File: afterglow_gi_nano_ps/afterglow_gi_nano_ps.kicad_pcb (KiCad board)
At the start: 2 copper layers, 84 x 134.5 mm, 69 parts, among them J1 Conn_02x17_Odd_Even, J2 POWER_CONN, J3 GI_WPC_J120, J4 GI_WPC_J121, J5 GI_CONN_J119, J6 Conn_01x12_Male, Q1 FQP30N06L, Q2 FQP30N06L, Q3 FQP30N06L, Q4 FQP30N06L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

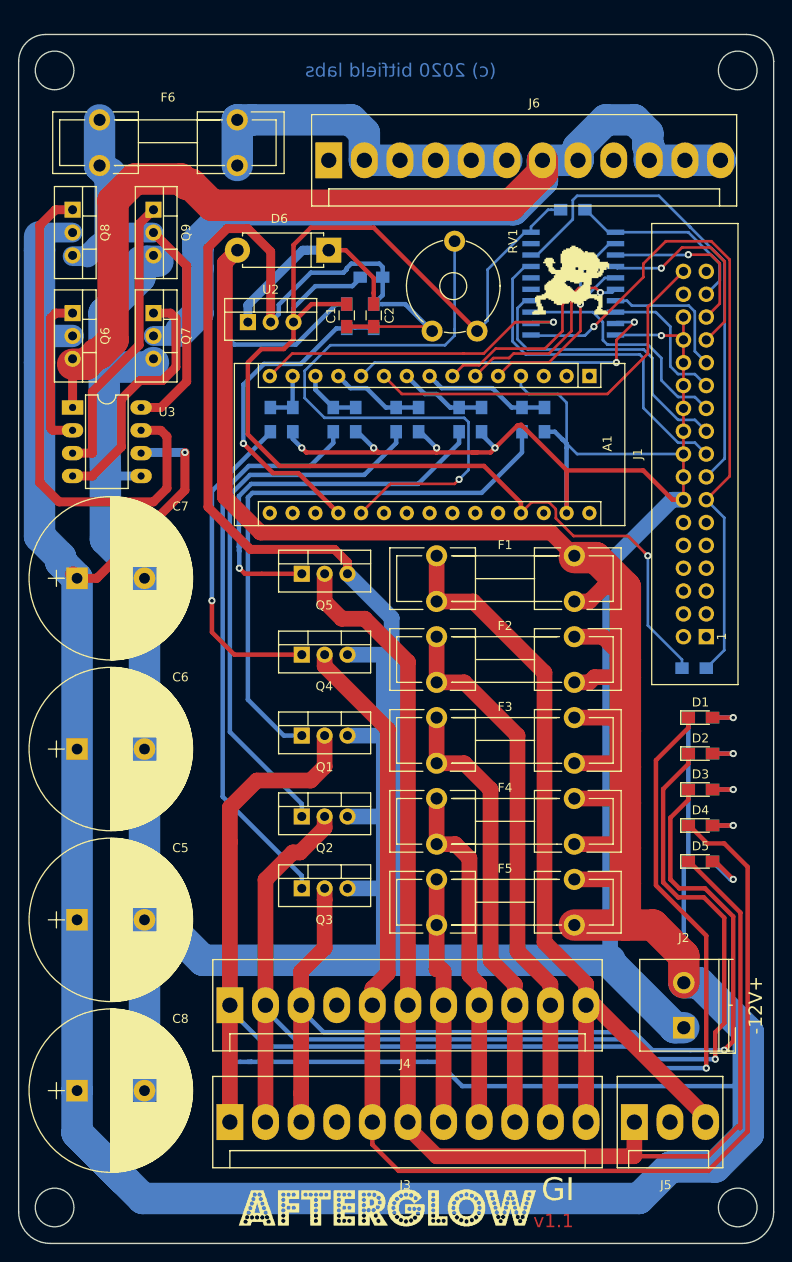
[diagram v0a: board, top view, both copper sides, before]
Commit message: New power supply
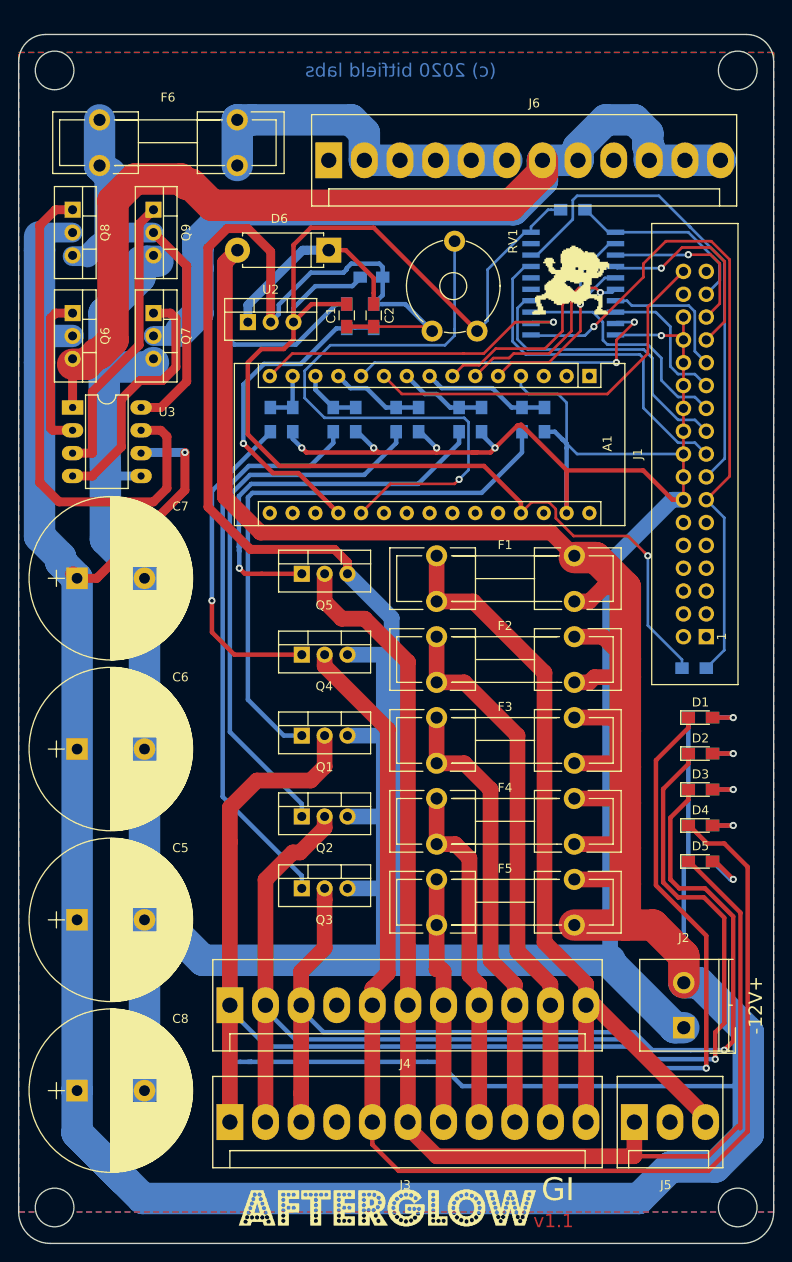
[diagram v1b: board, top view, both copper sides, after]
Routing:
- added copper zone on B.Cu, net GND
- added copper zone on F.Cu, net GND
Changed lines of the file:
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@@
   (segment (start 48.899999 32.100001) (end 50.5 30.5) (width 1) (layer F.Cu) (net 90))
   (segment (start 43.7 57.58) (end 43.7 50.764836) (width 1) (layer F.Cu) (net 90))
+  (zone (net 1) (net_name GND) (layer B.Cu) (hatch edge 0.508)
+    (connect_pads (clearance 0.508))
+    (min_thickness 0.254)
+    (fill yes (arc_segments 32) (thermal_gap 0.508) (thermal_bridge_width 0.508))
+    (polygon
+      (pts
+        (xy 119.5 142) (xy 35.5 142) (xy 35.5 13) (xy 119.5 13)
+      )
+    )
+  )
+  (zone (net 1) (net_name GND) (layer F.Cu) (hatch edge 0.508)
+    (connect_pads (clearance 0.508))
+    (min_thickness 0.254)
+    (fill yes (arc_segments 32) (thermal_gap 0.508) (thermal_bridge_width 0.508))
+    (polygon
+      (pts
+        (xy 119.5 142) (xy 35.5 142) (xy 35.5 13) (xy 119.5 13)
+      )
+    )
+  )
 )

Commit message: PCB cosmetix
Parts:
- F6 - 10A: renamed from F6
- J115 IN: renamed from J6
- J119 OUT: renamed from J5
- J120 OUT: renamed from J3
- J121 OUT: renamed from J4
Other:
- board text added: "2A"
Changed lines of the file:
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@@
   (general
     (thickness 1.6)
-    (drawings 16)
+    (drawings 21)
     (tracks 711)
     (zones 0)
@@
   )
   (setup
-    (last_trace_width 1)
+    (last_trace_width 0.5)
     (user_trace_width 1)
     (user_trace_width 1.75)
@@
     (pcbplotparams
       (layerselection 0x010fc_ffffffff)
-      (usegerberextensions false)
+      (usegerberextensions true)
       (usegerberattributes false)
       (usegerberadvancedattributes false)
@@
     (descr "Connector Headers with Friction Lock, 26-60-4020, http://www.molex.com/pdm_docs/sd/026604020_sd.pdf")
     (tags "connector molex kk_41791 26-60-4020")
-    (fp_text reference J6 (at 22.86 -6.35) (layer F.SilkS)
+    (fp_text reference "J115 IN" (at 22.5 -7) (layer F.SilkS)
       (effects (font (size 1 1) (thickness 0.15)))
     )
@@
     (descr "Fuseholder, 5x20, open, horizontal, Type-II, lateral,")
     (tags "Fuseholder 5x20 open horizontal Type-II lateral Sicherungshalter offen ")
-    (fp_text reference F6 (at 7.61 -2.5) (layer F.SilkS)
+    (fp_text reference "F6 - 10A" (at 7.61 -3) (layer F.SilkS)
       (effects (font (size 1 1) (thickness 0.15)))
     )
@@
     (descr "Connector Headers with Friction Lock, 26-60-4020, http://www.molex.com/pdm_docs/sd/026604020_sd.pdf")
     (tags "connector molex kk_41791 26-60-4020")
-    (fp_text reference J3 (at 19.5 7) (layer F.SilkS)
+    (fp_text reference "J120 OUT" (at 19.5 6.5) (layer F.SilkS)
       (effects (font (size 1 1) (thickness 0.15)))
     )
@@
     (descr "Connector Headers with Friction Lock, 26-60-4020, http://www.molex.com/pdm_docs/sd/026604020_sd.pdf")
     (tags "connector molex kk_41791 26-60-4020")
-    (fp_text reference J4 (at 19.5 6.5) (layer F.SilkS)
+    (fp_text reference "J121 OUT" (at 19.5 6.5) (layer F.SilkS)
       (effects (font (size 1 1) (thickness 0.15)))
     )
@@
     (descr "Connector Headers with Friction Lock, 26-60-4020, http://www.molex.com/pdm_docs/sd/026604020_sd.pdf")
     (tags "connector molex kk_41791 26-60-4020")
-    (fp_text reference J5 (at 3.5 7) (layer F.SilkS)
+    (fp_text reference "J119 OUT" (at 3.5 6.5) (layer F.SilkS)
       (effects (font (size 1 1) (thickness 0.15)))
     )
@@
       (xy 18.3 0)) (layer F.SilkS) (width 0.01))
   )
+  (gr_text 2A (at 89.5 106.5) (layer F.SilkS)
+    (effects (font (size 1 1) (thickness 0.15)))
+  )
+  (gr_text 2A (at 89.5 97.5) (layer F.SilkS)
+    (effects (font (size 1 1) (thickness 0.15)))
+  )
+  (gr_text 2A (at 89.5 88.5) (layer F.SilkS)
+    (effects (font (size 1 1) (thickness 0.15)))
+  )
+  (gr_text 2A (at 89.5 79.5) (layer F.SilkS)
+    (effects (font (size 1 1) (thickness 0.15)))
+  )
+  (gr_text 2A (at 89.5 70.5) (layer F.SilkS)
+    (effects (font (size 1 1) (thickness 0.15)))
+  )
   (dimension 84.001488 (width 0.3) (layer F.SilkS)

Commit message: Added missing C4 footprint, grounding pads
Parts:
- removed the ? at (39.5, 141.5)
- removed the ? at (115.5, 15.0)
- added C4: C, Capacitors_THT:C_Rect_L7.0mm_W3.5mm_P5.00mm, F.Cu at (60.0, 89.0)
- added REF**: MountingHole_4.3mm_M4_Pad, Mounting_Holes:MountingHole_4.3mm_M4_Pad, F.Cu at (115.0, 15.5)
- added REF**: MountingHole_4.3mm_M4_Pad, Mounting_Holes:MountingHole_4.3mm_M4_Pad, F.Cu at (40.0, 141.0)
- F6: renamed from F6 - 10A
- J3: renamed from J120 OUT
- J4: renamed from J121 OUT
- J5: renamed from J119 OUT
- J6: renamed from J115 IN
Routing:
- net +12V: track 551.1 -> 574.0 mm
- net GND: track 526.3 -> 539.5 mm
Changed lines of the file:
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@@
     (thickness 1.6)
     (drawings 21)
-    (tracks 711)
+    (tracks 718)
     (zones 0)
-    (modules 69)
+    (modules 70)
     (nets 91)
   )
@@
   )
   (setup
-    (last_trace_width 0.5)
+    (last_trace_width 1.75)
     (user_trace_width 1)
     (user_trace_width 1.75)
@@
     (add_net "Net-(F5-Pad1)")
   )
+  (module Mounting_Holes:MountingHole_4.3mm_M4_Pad (layer F.Cu)
+    (at 115 15.5)
+    (descr "Mounting Hole 4.3mm, M4")
+    (tags "mounting hole 4.3mm m4")
+    (fp_text reference REF** (at 0 -5.3) (layer F.SilkS)
+      (effects (font (size 1 1) (thickness 0.15)))
+    )
+    (fp_text value MountingHole_4.3mm_M4_Pad (at 0 5.3) (layer F.Fab)
+      (effects (font (size 1 1) (thickness 0.15)))
+    )
+    (fp_circle (center 0 0) (end 4.55 0) (layer F.CrtYd) (width 0.05))
+    (fp_circle (center 0 0) (end 4.3 0) (layer Cmts.User) (width 0.15))
+    (pad 1 thru_hole circle (at 0 0) (size 8.6 8.6) (drill 4.3) (layers *.Cu *.Mask))
+  )
+  (module Mounting_Holes:MountingHole_4.3mm_M4_Pad (layer F.Cu)
+    (at 40 141)
+    (descr "Mounting Hole 4.3mm, M4")
+    (tags "mounting hole 4.3mm m4")
+    (fp_text reference REF** (at 0 -5.3) (layer F.SilkS)
+      (effects (font (size 1 1) (thickness 0.15)))
+    )
+    (fp_text value MountingHole_4.3mm_M4_Pad (at 0 5.3) (layer F.Fab)
+      (effects (font (size 1 1) (thickness 0.15)))
+    )
+    (fp_circle (center 0 0) (end 4.55 0) (layer F.CrtYd) (width 0.05))
+    (fp_circle (center 0 0) (end 4.3 0) (layer Cmts.User) (width 0.15))
+    (pad 1 thru_hole circle (at 0 0) (size 8.6 8.6) (drill 4.3) (layers *.Cu *.Mask))
+  )
+  (module Capacitors_THT:C_Rect_L7.0mm_W3.5mm_P5.00mm (layer F.Cu)
+    (at 60 89 90)
+    (descr "C, Rect series, Radial, pin pitch=5.00mm, , length*width=7*3.5mm^2, Capacitor")
+    (tags "C Rect series Radial pin pitch 5.00mm  length 7mm width 3.5mm Capacitor")
+    (fp_text reference C4 (at 2.5 -3.06 90) (layer F.SilkS)
+      (effects (font (size 1 1) (thickness 0.15)))
+    )
+    (fp_text value C (at 2.5 3.06 90) (layer F.Fab)
+      (effects (font (size 1 1) (thickness 0.15)))
+    )
+    (fp_text user %R (at 2.5 0 90) (layer F.Fab)
+      (effects (font (size 1 1) (thickness 0.15)))
+    )
+    (fp_line (start 6.35 -2.1) (end -1.35 -2.1) (layer F.CrtYd) (width 0.05))
+    (fp_line (start 6.35 2.1) (end 6.35 -2.1) (layer F.CrtYd) (width 0.05))
+    (fp_line (start -1.35 2.1) (end 6.35 2.1) (layer F.CrtYd) (width 0.05))
+    (fp_line (start -1.35 -2.1) (end -1.35 2.1) (layer F.CrtYd) (width 0.05))
+    (fp_line (start 6.06 -1.81) (end 6.06 1.81) (layer F.SilkS) (width 0.12))
+    (fp_line (start -1.06 -1.81) (end -1.06 1.81) (layer F.SilkS) (width 0.12))
+    (fp_line (start -1.06 1.81) (end 6.06 1.81) (layer F.SilkS) (width 0.12))
+    (fp_line (start -1.06 -1.81) (end 6.06 -1.81) (layer F.SilkS) (width 0.12))
+    (fp_line (start 6 -1.75) (end -1 -1.75) (layer F.Fab) (width 0.1))
+    (fp_line (start 6 1.75) (end 6 -1.75) (layer F.Fab) (width 0.1))
+    (fp_line (start -1 1.75) (end 6 1.75) (layer F.Fab) (width 0.1))
+    (fp_line (start -1 -1.75) (end -1 1.75) (layer F.Fab) (width 0.1))
+    (pad 2 thru_hole circle (at 5 0 90) (size 1.6 1.6) (drill 0.8) (layers *.Cu *.Mask)
+      (net 1 GND))
+    (pad 1 thru_hole circle (at 0 0 90) (size 1.6 1.6) (drill 0.8) (layers *.Cu *.Mask)
+      (net 3 +12V))
+    (model ${KISYS3DMOD}/Capacitors_THT.3dshapes/C_Rect_L7.0mm_W3.5mm_P5.00mm.wrl
+      (at (xyz 0 0 0))
+      (scale (xyz 1 1 1))
+      (rotate (xyz 0 0 0))
+    )
+  )
   (module Housings_DIP:DIP-8_W7.62mm_LongPads (layer F.Cu)
     (at 41.5 52.5)
@@
     (descr "Connector Headers with Friction Lock, 26-60-4020, http://www.molex.com/pdm_docs/sd/026604020_sd.pdf")
     (tags "connector molex kk_41791 26-60-4020")
-    (fp_text reference "J115 IN" (at 22.5 -7) (layer F.SilkS)
+    (fp_text reference J6 (at 22.5 -7) (layer F.SilkS)
       (effects (font (size 1 1) (thickness 0.15)))
     )
@@
     (descr "Fuseholder, 5x20, open, horizontal, Type-II, lateral,")
     (tags "Fuseholder 5x20 open horizontal Type-II lateral Sicherungshalter offen ")
-    (fp_text reference "F6 - 10A" (at 7.61 -3) (layer F.SilkS)
+    (fp_text reference F6 (at 7.61 -3) (layer F.SilkS)
       (effects (font (size 1 1) (thickness 0.15)))
     )
@@
   )
   (module Mounting_Holes:MountingHole_4.3mm_M4_DIN965 (layer F.Cu)
-    (at 39.5 141.5)
-    (descr "Mounting Hole 4.3mm, no annular, M4, DIN965")
-    (tags "mounting hole 4.3mm no annular m4 din965")
-    (fp_text reference "" (at 0 -4.75) (layer F.SilkS)
-      (effects (font (size 1 1) (thickness 0.15)))
-    )
-    (fp_text value MountingHole_4.3mm_M4_DIN965 (at 0 4.75) (layer F.Fab)
-      (effects (font (size 1 1) (thickness 0.15)))
-    )
-    (fp_circle (center 0 0) (end 4 0) (layer F.CrtYd) (width 0.05))
-    (fp_circle (center 0 0) (end 3.75 0) (layer Cmts.User) (width 0.15))
-    (pad 1 np_thru_hole circle (at 0 0) (size 4.3 4.3) (drill 4.3) (layers *.Cu *.Mask))
-  )
-  (module Mounting_Holes:MountingHole_4.3mm_M4_DIN965 (layer F.Cu)
     (at 115.5 141.5)
     (descr "Mounting Hole 4.3mm, no annular, M4, DIN965")
@@
     (descr "Connector Headers with Friction Lock, 26-60-4020, http://www.molex.com/pdm_docs/sd/026604020_sd.pdf")
     (tags "connector molex kk_41791 26-60-4020")
-    (fp_text reference "J120 OUT" (at 19.5 6.5) (layer F.SilkS)
+    (fp_text reference J3 (at 19.5 6.5) (layer F.SilkS)
       (effects (font (size 1 1) (thickness 0.15)))
     )
@@
     (descr "Connector Headers with Friction Lock, 26-60-4020, http://www.molex.com/pdm_docs/sd/026604020_sd.pdf")
     (tags "connector molex kk_41791 26-60-4020")
-    (fp_text reference "J121 OUT" (at 19.5 6.5) (layer F.SilkS)
+    (fp_text reference J4 (at 19.5 6.5) (layer F.SilkS)
       (effects (font (size 1 1) (thickness 0.15)))
     )
@@
     (descr "Connector Headers with Friction Lock, 26-60-4020, http://www.molex.com/pdm_docs/sd/026604020_sd.pdf")
     (tags "connector molex kk_41791 26-60-4020")
-    (fp_text reference "J119 OUT" (at 3.5 6.5) (layer F.SilkS)
+    (fp_text reference J5 (at 3.5 6.5) (layer F.SilkS)
       (effects (font (size 1 1) (thickness 0.15)))
     )
@@
     )
   )
-  (module Mounting_Holes:MountingHole_4.3mm_M4_DIN965 (layer F.Cu)
-    (at 115.5 15)
-    (descr "Mounting Hole 4.3mm, no annular, M4, DIN965")
-    (tags "mounting hole 4.3mm no annular m4 din965")
-    (fp_text reference "" (at 0 -4.75) (layer F.SilkS)
-      (effects (font (size 1 1) (thickness 0.15)))
-    )
-    (fp_text value MountingHole_4.3mm_M4_DIN965 (at 0 4.75) (layer F.Fab)
-      (effects (font (size 1 1) (thickness 0.15)))
-    )
-    (fp_circle (center 0 0) (end 4 0) (layer F.CrtYd) (width 0.05))
-    (fp_circle (center 0 0) (end 3.75 0) (layer Cmts.User) (width 0.15))
-    (pad 1 np_thru_hole circle (at 0 0) (size 4.3 4.3) (drill 4.3) (layers *.Cu *.Mask))
-  )
   (module FLAKIE:FLAKIE_inv (layer F.Cu)
     (at 92.5 34.5)
@@
   (segment (start 49.12 60.12) (end 45.294351 60.12) (width 1) (layer B.Cu) (net 1))
   (segment (start 45.152328 59.977977) (end 45 48) (width 3.5) (layer B.Cu) (net 1))
+  (segment (start 56 84) (end 49.5 90.5) (width 1.75) (layer F.Cu) (net 1))
+  (segment (start 60 84) (end 56 84) (width 1.75) (layer F.Cu) (net 1))
   (segment (start 68.08 41) (end 66.08 43) (width 0.5) (layer F.Cu) (net 2))
   (segment (start 72 41) (end 68.08 41) (width 0.5) (layer F.Cu) (net 2))
@@
   (segment (start 49.2 57.5) (end 49.12 57.58) (width 1) (layer B.Cu) (net 3))
   (segment (start 54 57.5) (end 49.2 57.5) (width 1) (layer B.Cu) (net 3))
+  (segment (start 42 91.5) (end 42 90.5) (width 1.75) (layer F.Cu) (net 3))
+  (segment (start 45.5 95) (end 42 91.5) (width 1.75) (layer F.Cu) (net 3))
+  (segment (start 52.5 95) (end 45.5 95) (width 1.75) (layer F.Cu) (net 3))
+  (segment (start 60 89) (end 58.5 89) (width 1.75) (layer F.Cu) (net 3))
+  (segment (start 58.5 89) (end 52.5 95) (width 1.75) (layer F.Cu) (net 3))
   (via (at 115 87) (size 0.8) (drill 0.4) (layers F.Cu B.Cu) (net 4))
   (segment (start 112.7 87) (end 115 87) (width 0.5) (layer F.Cu) (net 4))
@@
       )
     )
+  )
+  (zone (net 1) (net_name GND) (layer F.Cu) (hatch edge 0.508)
+    (connect_pads (clearance 0.508))
+    (min_thickness 0.254)
+    (fill yes (arc_segments 32) (thermal_gap 0.508) (thermal_bridge_width 0.508))
+    (polygon
+      (pts
+        (xy 119.5 141) (xy 119 143.5) (xy 117.5 145) (xy 116 145.5) (xy 109.5 145.5)
+        (xy 109.5 140) (xy 113.5 138.5) (xy 119.5 137.5)
+      )
+    )
+  )
+  (zone (net 1) (net_name GND) (layer F.Cu) (hatch edge 0.508)
+    (connect_pads (clearance 0.508))
+    (min_thickness 0.254)
+    (fill yes (arc_segments 32) (thermal_gap 0.508) (thermal_bridge_width 0.508))
+    (polygon
+      (pts
+        (xy 111 139.5) (xy 111 145.5) (xy 38.5 145.5) (xy 37.5 145) (xy 36 143.5)
+        (xy 35.5 141.5) (xy 35.5 138.5)
+      )
+    )
+  )
+  (zone (net 1) (net_name GND) (layer F.Cu) (hatch edge 0.508)
+    (connect_pads (clearance 0.508))
+    (min_thickness 0.254)
+    (fill yes (arc_segments 32) (thermal_gap 0.508) (thermal_bridge_width 0.508))
+    (polygon
+      (pts
+        (xy 118 11.5) (xy 119 12.5) (xy 119.5 14.5) (xy 119.5 18) (xy 35.5 18)
+        (xy 35.5 13.5) (xy 37 11.5) (xy 40.5 11) (xy 116.5 11)
+      )
+    )
